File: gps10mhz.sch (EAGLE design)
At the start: 40 parts, among them IC2 7803.3, IC3 CD74HC132E, U1 BB3553AM

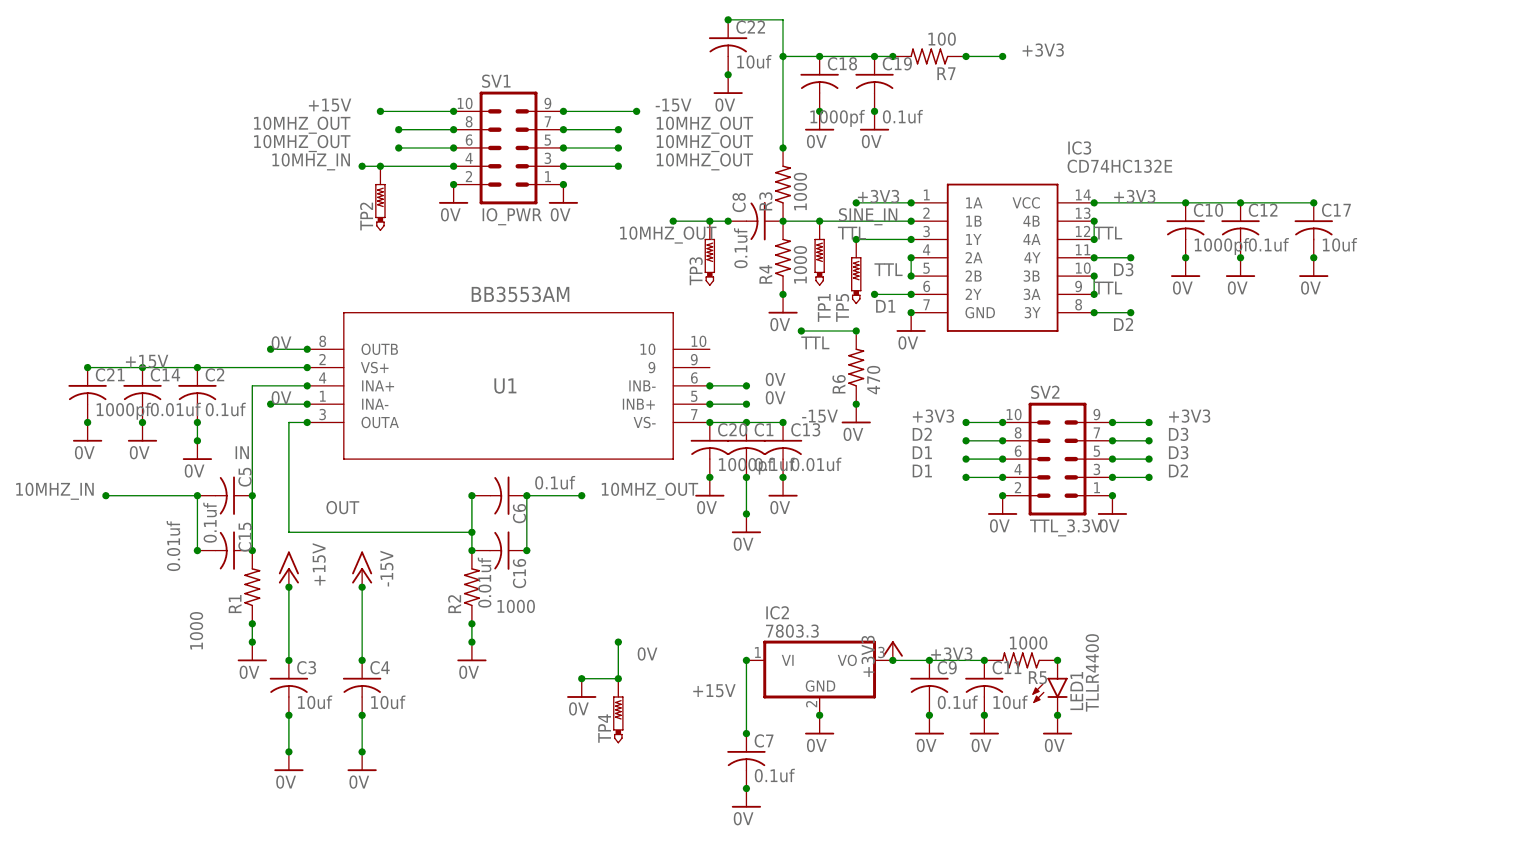
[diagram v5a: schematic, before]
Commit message: 3.3 digital only version
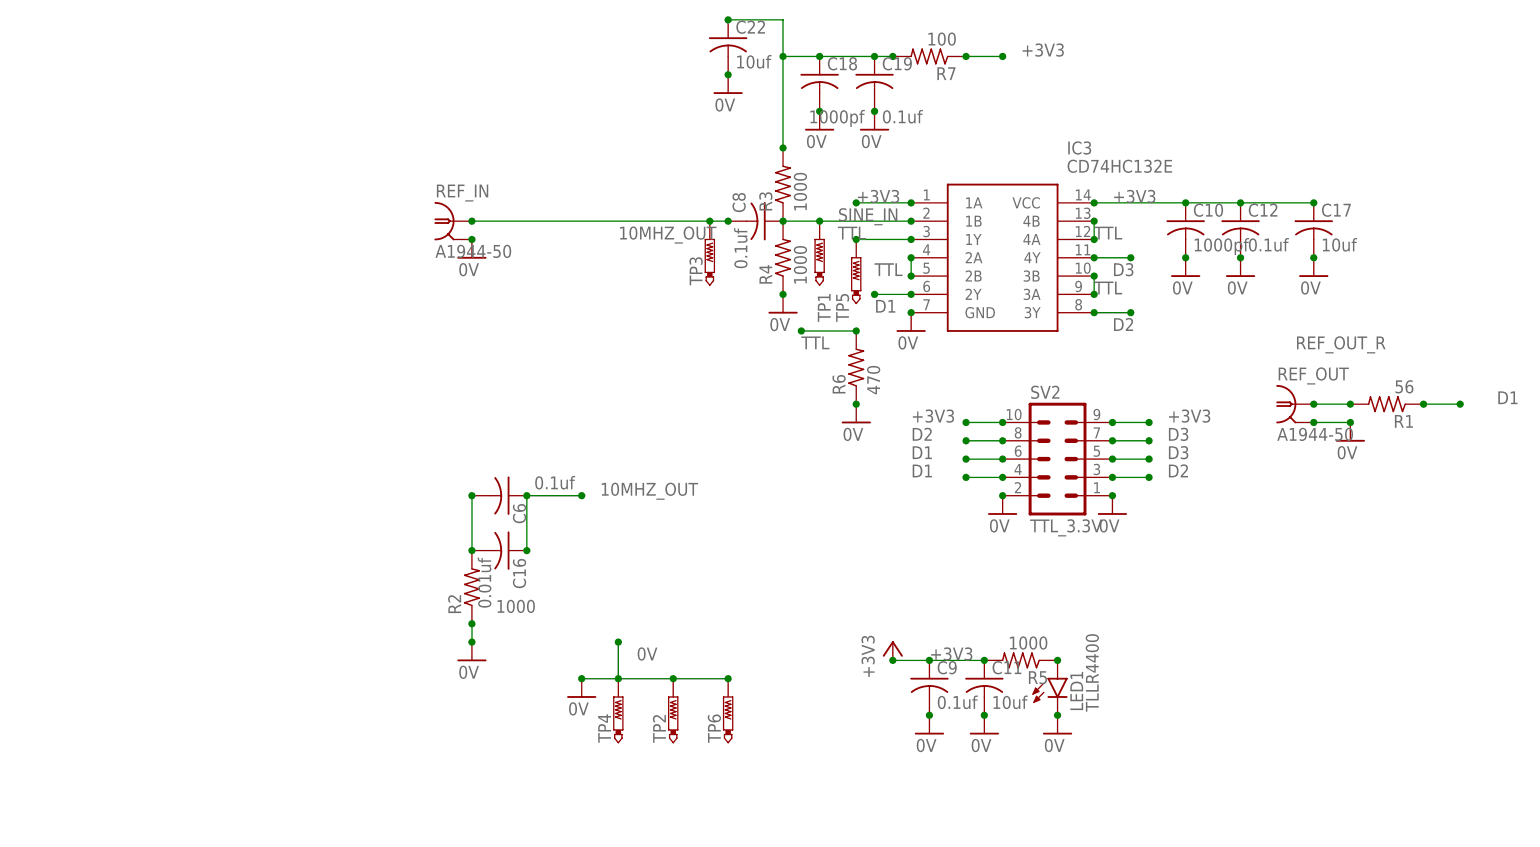
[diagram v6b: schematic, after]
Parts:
- removed C1, C2, C5, C7: 0.1uf, rcl:C-USC0805
- removed C13, C14, C15: 0.01uf, rcl:C-USC0805
- removed C20, C21: 1000pf, rcl:C-USC0805
- removed C3, C4: 10uf, rcl:C-USC0805
- removed IC2: 7803.3, linear:7805T
- removed SV1: IO_PWR, con-lstb:MA05-2
- removed U1: BB3553AM, 2025-01-01_18-24-55_Library:OPA2541AMBB3553AM
- added REF_IN, REF_OUT: A1944-50, con-coax:A1944-50
- added TP6: PTR1PAD1-13, testpad:PTR1PAD1-13
- R1: value 1000 -> 56
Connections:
- removed net +15V: C14.1, C2.1, C21.1, C3.1, C7.1, IC2.VI, SV1.10, U1.VS+
- removed net -15V: C1.1, C13.1, C20.1, C4.1, SV1.9, U1.VS-
- removed net 10MHZ_IN: C15.2, C5.2, SV1.4, TP2.TP
- removed net IN: C15.1, C5.1, R1.2, U1.INA+
- new net REF_OUT_R: R1.2, REF_OUT.1
- net +3V3: no longer IC2.VO
- net 0V: now also REF_IN.2, REF_OUT.2, TP2.TP, TP6.TP; no longer C1.2, C13.2, C14.2, C2.2, C20.2, C21.2, C3.2, C4.2, C7.2, IC2.GND, R1.1, SV1.1, SV1.2, U1.INA-, U1.INB+, U1.INB-, U1.OUTB
- net 10MHZ_OUT: now also REF_IN.1; no longer SV1.3, SV1.5, SV1.6, SV1.7, SV1.8
- net D1: now also R1.1
- net OUT: no longer U1.OUTA
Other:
- moved on the sheet: R1, TP2

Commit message: up
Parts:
- R1: value 56 -> 22
- R3: value 1000 -> 910
- R7: value 100 -> 130
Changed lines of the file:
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@@
 <part name="GND14" library="supply1" library_urn="urn:adsk.eagle:library:371" deviceset="0V" device=""/>
 <part name="C8" library="rcl" library_urn="urn:adsk.eagle:library:334" deviceset="C-US" device="C0805" package3d_urn="urn:adsk.eagle:package:23617/2" value="0.1uf"/>
-<part name="R3" library="rcl" library_urn="urn:adsk.eagle:library:334" deviceset="R-US_" device="R1206" package3d_urn="urn:adsk.eagle:package:23540/2" value="1000"/>
+<part name="R3" library="rcl" library_urn="urn:adsk.eagle:library:334" deviceset="R-US_" device="R1206" package3d_urn="urn:adsk.eagle:package:23540/2" value="910"/>
 <part name="R4" library="rcl" library_urn="urn:adsk.eagle:library:334" deviceset="R-US_" device="R1206" package3d_urn="urn:adsk.eagle:package:23540/2" value="1000"/>
 <part name="GND15" library="supply1" library_urn="urn:adsk.eagle:library:371" deviceset="0V" device=""/>
@@
 <part name="GND23" library="supply1" library_urn="urn:adsk.eagle:library:371" deviceset="0V" device=""/>
 <part name="C17" library="rcl" library_urn="urn:adsk.eagle:library:334" deviceset="C-US" device="C0805" package3d_urn="urn:adsk.eagle:package:23617/2" value="10uf"/>
-<part name="R7" library="rcl" library_urn="urn:adsk.eagle:library:334" deviceset="R-US_" device="R1206" package3d_urn="urn:adsk.eagle:package:23540/2" value="100"/>
+<part name="R7" library="rcl" library_urn="urn:adsk.eagle:library:334" deviceset="R-US_" device="R1206" package3d_urn="urn:adsk.eagle:package:23540/2" value="130"/>
 <part name="C18" library="rcl" library_urn="urn:adsk.eagle:library:334" deviceset="C-US" device="C0805" package3d_urn="urn:adsk.eagle:package:23617/2" value="1000pf"/>
 <part name="C19" library="rcl" library_urn="urn:adsk.eagle:library:334" deviceset="C-US" device="C0805" package3d_urn="urn:adsk.eagle:package:23617/2" value="0.1uf"/>
@@
 <part name="GND2" library="supply1" library_urn="urn:adsk.eagle:library:371" deviceset="0V" device=""/>
 <part name="REF_OUT" library="con-coax" library_urn="urn:adsk.eagle:library:133" deviceset="A1944-50" device="" package3d_urn="urn:adsk.eagle:package:6200/1"/>
-<part name="R1" library="rcl" library_urn="urn:adsk.eagle:library:334" deviceset="R-US_" device="R1206" package3d_urn="urn:adsk.eagle:package:23540/2" value="56"/>
+<part name="R1" library="rcl" library_urn="urn:adsk.eagle:library:334" deviceset="R-US_" device="R1206" package3d_urn="urn:adsk.eagle:package:23540/2" value="22"/>
 <part name="GND3" library="supply1" library_urn="urn:adsk.eagle:library:371" deviceset="0V" device=""/>
 <part name="TP2" library="testpad" library_urn="urn:adsk.eagle:library:385" deviceset="PTR1" device="PAD1-13" package3d_urn="urn:adsk.eagle:package:27946/1"/>
